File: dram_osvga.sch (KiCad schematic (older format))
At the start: 2 parts

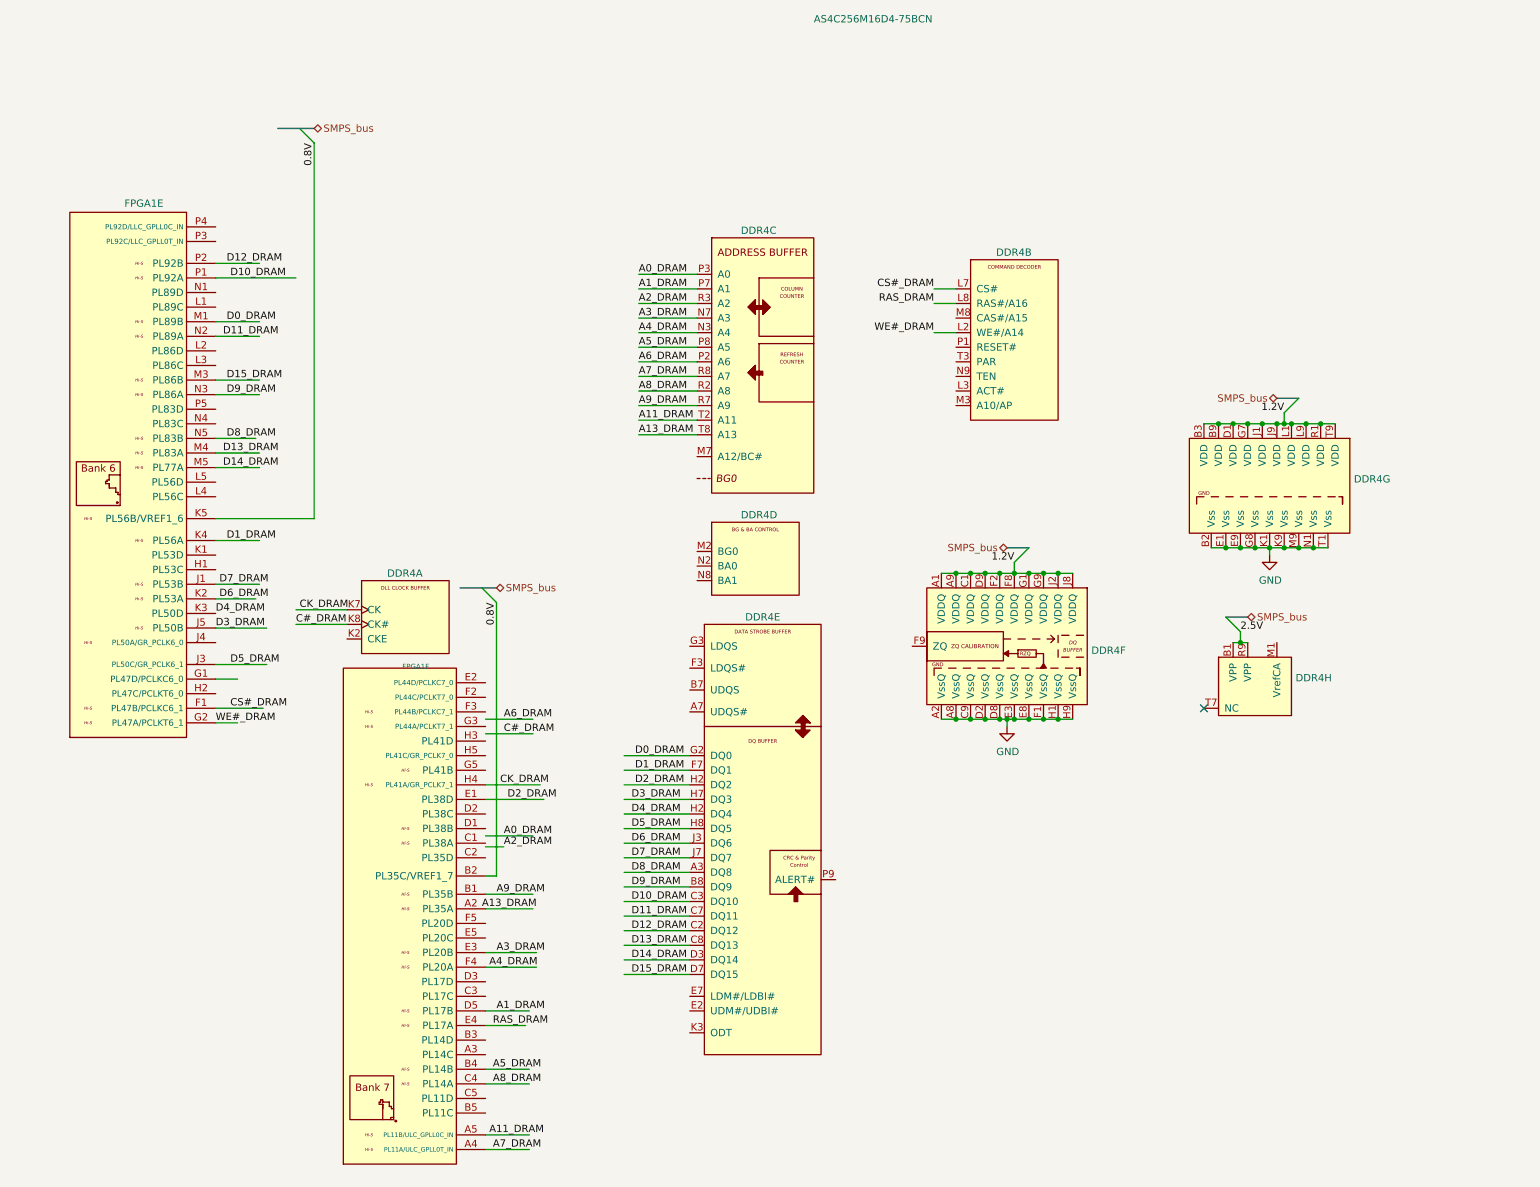
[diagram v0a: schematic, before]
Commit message: Add files via upload
Added Pull-up and pull-down resistors for JTAG and sysConfig connections.
Added pinheaders for FPGA-Configuration. (replacing edge-connector)
Combined the DVI+VGA and USB-C hierarchical sheets into one.
Assigned a dedicated sheet for the DAC.
Added 75 Ohm terminal-resistors to output of DAC.
Placed filtering-capacitors for DAC VAA.
Connected VGA ID-bits and DVI DDC together.
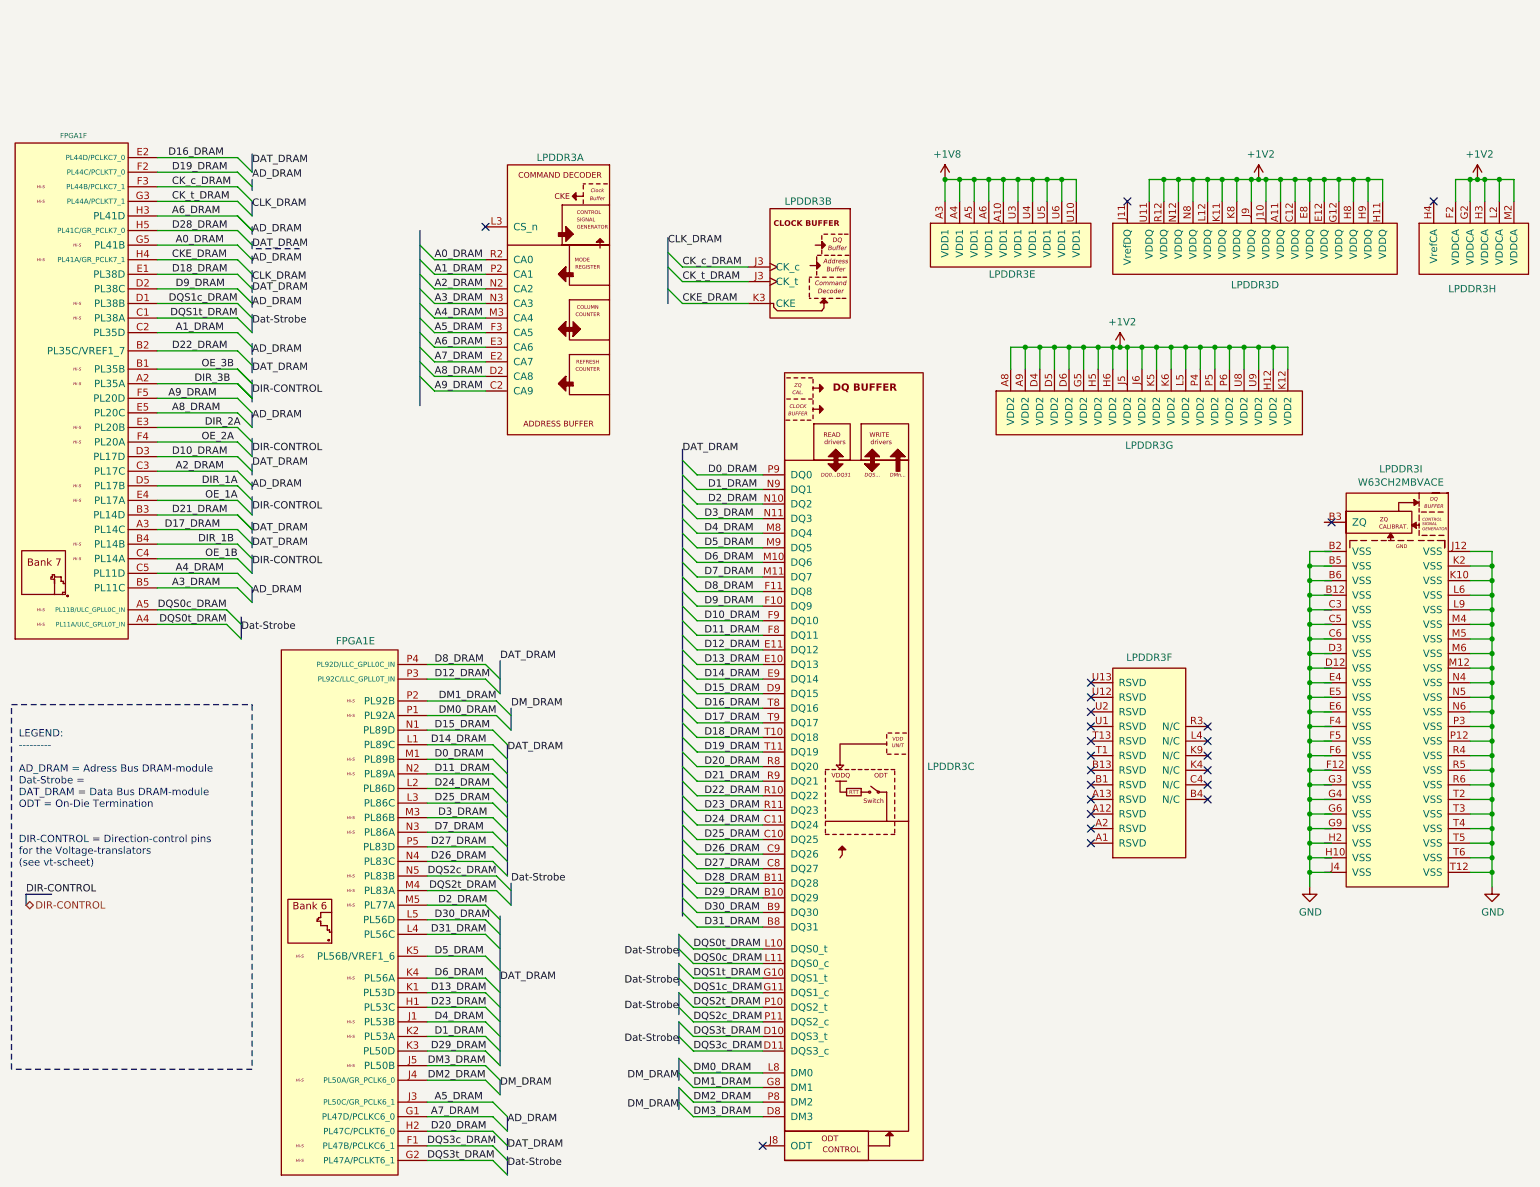
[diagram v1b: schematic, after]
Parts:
- removed DDR4: AS4C256M16D4-75BCN, Package_BGA:FBGA-96-Alliance_, symbol LRJ-parts:AS4C256M16D4-75BCN
- added LPDDR3: W63CH2MBVACE, Package_BGA:Winbond_VFBGA-178_W63CH2MBVACE, symbol LRJ-parts:W63CH2MBVACE
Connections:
- net labels added: +1V2, +1V8, AD_DRAM, CKE_DRAM, CK_c_DRAM, CK_t_DRAM, CLK_DRAM, D16_DRAM, D17_DRAM, D18_DRAM, D19_DRAM, D20_DRAM, D21_DRAM, D22_DRAM, D23_DRAM, D24_DRAM, D25_DRAM, D26_DRAM, D27_DRAM, D28_DRAM, D29_DRAM, D30_DRAM, D31_DRAM, DAT_DRAM, DIR-CONTROL, DIR_1A, DIR_1B, DIR_2A, DIR_3B, DM0_DRAM, DM1_DRAM, DM2_DRAM, DM3_DRAM, DM_DRAM, DQS0c_DRAM, DQS0t_DRAM, DQS1c_DRAM, DQS1t_DRAM, DQS2c_DRAM, DQS2t_DRAM, DQS3c_DRAM, DQS3t_DRAM, Dat-Strobe, OE_1A, OE_1B, OE_2A, OE_3B
- net labels removed: 0.8V, 1.2V, 2.5V, A11_DRAM, A13_DRAM, C#_DRAM, CK_DRAM, CS#_DRAM, RAS_DRAM, SMPS_bus, WE#_DRAM
- wire segments 114 -> 317
- no-connect marks 1 -> 23
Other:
- note added: "LEGEND:\n---------\n\nAD_DRAM = Adress Bus DRAM-module\nDat-Strobe = \nDAT_DRAM = Data Bus DRAM-module\nODT = On-Die Termination\n\n\nDIR-CONTROL = Direction-control pins \nfor the Voltage-translators \n(see vt-scheet)\n\n"
- moved on the sheet: FPGA1E, FPGA1F

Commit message: Add files via upload
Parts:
- added RZQ1: ERJ-8ENF2400V, Resistor_SMD:R_Panasonic_1206_3216Metric_ERJ8EN_HandSolder, symbol LRJ-parts:ERJ-8ENF2400V
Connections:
- net labels added: CON_DRAM, CS_DRAM, ODT_DRAM
- wire segments 317 -> 320
- no-connect marks 23 -> 20
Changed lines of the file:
@@
 $EndComp
 Wire Wire Line
-	9550 3450 9700 3450
-Wire Wire Line
-	9550 3550 9700 3550
-Wire Wire Line
-	9550 3650 9700 3650
-Wire Wire Line
-	9550 3750 9700 3750
-Wire Wire Line
-	9550 3850 9700 3850
-Wire Wire Line
-	9550 3950 9700 3950
-Wire Wire Line
-	9550 4050 9700 4050
-Wire Wire Line
-	9550 4150 9700 4150
-Wire Wire Line
-	9550 4250 9700 4250
-Wire Wire Line
-	9550 4350 9700 4350
-Wire Wire Line
-	9550 4450 9700 4450
-Wire Wire Line
-	9550 4550 9700 4550
-Wire Wire Line
-	9550 4650 9700 4650
-Wire Wire Line
-	9550 4750 9700 4750
-Wire Wire Line
-	9550 4850 9700 4850
-Wire Wire Line
-	9550 4950 9700 4950
-Wire Wire Line
-	9550 5050 9700 5050
-Wire Wire Line
-	9550 5150 9700 5150
-Wire Wire Line
-	9550 5250 9700 5250
-Wire Wire Line
-	9550 5350 9700 5350
-Wire Wire Line
-	9550 5450 9700 5450
-Wire Wire Line
-	9550 5550 9700 5550
-Wire Wire Line
-	9550 5650 9700 5650
+	9500 3450 9650 3450
+Wire Wire Line
+	9500 3550 9650 3550
+Wire Wire Line
+	9500 3650 9650 3650
+Wire Wire Line
+	9500 3750 9650 3750
+Wire Wire Line
+	9500 3850 9650 3850
+Wire Wire Line
+	9500 3950 9650 3950
+Wire Wire Line
+	9500 4050 9650 4050
+Wire Wire Line
+	9500 4150 9650 4150
+Wire Wire Line
+	9500 4250 9650 4250
+Wire Wire Line
+	9500 4350 9650 4350
+Wire Wire Line
+	9500 4450 9650 4450
+Wire Wire Line
+	9500 4550 9650 4550
+Wire Wire Line
+	9500 4650 9650 4650
+Wire Wire Line
+	9500 4750 9650 4750
+Wire Wire Line
+	9500 4850 9650 4850
+Wire Wire Line
+	9500 4950 9650 4950
+Wire Wire Line
+	9500 5050 9650 5050
+Wire Wire Line
+	9500 5150 9650 5150
+Wire Wire Line
+	9500 5250 9650 5250
+Wire Wire Line
+	9500 5350 9650 5350
+Wire Wire Line
+	9500 5450 9650 5450
+Wire Wire Line
+	9500 5550 9650 5550
+Wire Wire Line
+	9500 5650 9650 5650
 Wire Wire Line
 	10650 3450 10800 3450
@@
 L power:GND #PWR0130
 U 1 1 5FC20D0A
-P 9550 5750
-F 0 "#PWR0130" H 9550 5500 50  0001 C CNN
-F 1 "GND" H 9555 5577 50  0000 C CNN
-F 2 "" H 9550 5750 50  0001 C CNN
-F 3 "" H 9550 5750 50  0001 C CNN
-	1    9550 5750
+P 9500 5750
+F 0 "#PWR0130" H 9500 5500 50  0001 C CNN
+F 1 "GND" H 9505 5577 50  0000 C CNN
+F 2 "" H 9500 5750 50  0001 C CNN
+F 3 "" H 9500 5750 50  0001 C CNN
+	1    9500 5750
 	1    0    0    -1
 $EndComp
@@
 $EndComp
 Wire Wire Line
-	9550 3450 9550 3550
-Connection ~ 9550 3550
-Wire Wire Line
-	9550 3550 9550 3650
-Connection ~ 9550 3650
-Wire Wire Line
-	9550 3650 9550 3750
-Connection ~ 9550 3750
-Wire Wire Line
-	9550 3750 9550 3850
-Connection ~ 9550 3850
-Wire Wire Line
-	9550 3850 9550 3950
-Connection ~ 9550 3950
-Wire Wire Line
-	9550 3950 9550 4050
-Connection ~ 9550 4050
-Wire Wire Line
-	9550 4050 9550 4150
-Connection ~ 9550 4150
-Wire Wire Line
-	9550 4150 9550 4250
-Connection ~ 9550 4250
-Wire Wire Line
-	9550 4250 9550 4350
-Connection ~ 9550 4350
-Wire Wire Line
-	9550 4350 9550 4450
-Connection ~ 9550 4450
-Wire Wire Line
-	9550 4450 9550 4550
-Connection ~ 9550 4550
-Wire Wire Line
-	9550 4550 9550 4650
-Connection ~ 9550 4650
-Wire Wire Line
-	9550 4650 9550 4750
-Connection ~ 9550 4750
-Wire Wire Line
-	9550 4750 9550 4850
-Connection ~ 9550 4850
-Wire Wire Line
-	9550 4850 9550 4950
-Connection ~ 9550 4950
-Wire Wire Line
-	9550 4950 9550 5050
-Connection ~ 9550 5050
-Wire Wire Line
-	9550 5050 9550 5150
-Connection ~ 9550 5150
-Wire Wire Line
-	9550 5150 9550 5250
-Connection ~ 9550 5250
-Wire Wire Line
-	9550 5250 9550 5350
-Connection ~ 9550 5350
-Wire Wire Line
-	9550 5350 9550 5450
-Connection ~ 9550 5450
-Wire Wire Line
-	9550 5450 9550 5550
-Connection ~ 9550 5550
-Wire Wire Line
-	9550 5550 9550 5650
-Connection ~ 9550 5650
-Wire Wire Line
-	9550 5650 9550 5750
+	9500 3450 9500 3550
+Connection ~ 9500 3550
+Wire Wire Line
+	9500 3550 9500 3650
+Connection ~ 9500 3650
+Wire Wire Line
+	9500 3650 9500 3750
+Connection ~ 9500 3750
+Wire Wire Line
+	9500 3750 9500 3850
+Connection ~ 9500 3850
+Wire Wire Line
+	9500 3850 9500 3950
+Connection ~ 9500 3950
+Wire Wire Line
+	9500 3950 9500 4050
+Connection ~ 9500 4050
+Wire Wire Line
+	9500 4050 9500 4150
+Connection ~ 9500 4150
+Wire Wire Line
+	9500 4150 9500 4250
+Connection ~ 9500 4250
+Wire Wire Line
+	9500 4250 9500 4350
+Connection ~ 9500 4350
+Wire Wire Line
+	9500 4350 9500 4450
+Connection ~ 9500 4450
+Wire Wire Line
+	9500 4450 9500 4550
+Connection ~ 9500 4550
+Wire Wire Line
+	9500 4550 9500 4650
+Connection ~ 9500 4650
+Wire Wire Line
+	9500 4650 9500 4750
+Connection ~ 9500 4750
+Wire Wire Line
+	9500 4750 9500 4850
+Connection ~ 9500 4850
+Wire Wire Line
+	9500 4850 9500 4950
+Connection ~ 9500 4950
+Wire Wire Line
+	9500 4950 9500 5050
+Connection ~ 9500 5050
+Wire Wire Line
+	9500 5050 9500 5150
+Connection ~ 9500 5150
+Wire Wire Line
+	9500 5150 9500 5250
+Connection ~ 9500 5250
+Wire Wire Line
+	9500 5250 9500 5350
+Connection ~ 9500 5350
+Wire Wire Line
+	9500 5350 9500 5450
+Connection ~ 9500 5450
+Wire Wire Line
+	9500 5450 9500 5550
+Connection ~ 9500 5550
+Wire Wire Line
+	9500 5550 9500 5650
+Connection ~ 9500 5650
+Wire Wire Line
+	9500 5650 9500 5750
 Wire Wire Line
 	10800 3450 10800 3550
@@
 L power:+1V8 #PWR0167
 U 1 1 608605CF
-P 7050 900
-F 0 "#PWR0167" H 7050 750 50  0001 C CNN
-F 1 "+1V8" H 7065 1073 50  0000 C CNN
-F 2 "" H 7050 900 50  0001 C CNN
-F 3 "" H 7050 900 50  0001 C CNN
-	1    7050 900
+P 6975 900
+F 0 "#PWR0167" H 6975 750 50  0001 C CNN
+F 1 "+1V8" H 6990 1073 50  0000 C CNN
+F 2 "" H 6975 900 50  0001 C CNN
+F 3 "" H 6975 900 50  0001 C CNN
+	1    6975 900
 	1    0    0    -1
 $EndComp
@@
 NoConn ~ 8050 5350
 NoConn ~ 8050 5450
-NoConn ~ 3900 1225
-NoConn ~ 5800 7525
-NoConn ~ 9700 3250
 NoConn ~ 10400 1050
 Wire Wire Line
@@
 Text Label 2300 1100 0    50   ~ 0
 CLK_DRAM
-Text Label 2300 900  0    50   ~ 0
-AD_DRAM
 Entry Wire Line
 	2200 850  2300 950
@@
 Wire Wire Line
 	1650 850  2200 850
-Wire Bus Line
-	2300 1050 2300 1150
 Entry Wire Line
 	2200 1250 2300 1350
@@
 Entry Wire Line
 	2200 3200 2300 3300
-Wire Notes Line
-	2325 1375 2625 1375
 Entry Wire Line
 	3950 5075 4050 5175
@@
 Wire Wire Line
 	1650 750  2200 750
-Wire Bus Line
-	2300 725  2300 850
 Text Label 2300 800  0    50   ~ 0
 DAT_DRAM
@@
 	7150 1050 7150 900
 Wire Wire Line
-	7150 900  7250 900
-Connection ~ 7250 900
-Wire Wire Line
 	7250 1050 7250 900
-Wire Wire Line
-	7250 900  7350 900
-Connection ~ 7350 900
 Wire Wire Line
 	7350 1050 7350 900
@@
 Wire Wire Line
 	7650 1050 7650 900
-Connection ~ 7150 900
-Connection ~ 7050 900
 Wire Wire Line
 	7050 900  7150 900
@@
 Text Label 2300 2375 0    50   ~ 0
 DIR-CONTROL
+$Comp
+L LRJ-parts:ERJ-8ENF2400V RZQ1
+U 1 1 5FADDD26
+P 9450 3250
+F 0 "RZQ1" H 9450 3250 39  0000 C CNN
+F 1 "ERJ-8ENF2400V" H 9450 3450 45  0000 C CNN
+F 2 "Resistor_SMD:R_Panasonic_1206_3216Metric_ERJ8EN_HandSolder" H 9450 3400 20  0001 C CNN
+F 3 "https://industrial.panasonic.com/cdbs/www-data/pdf/RDA0000/AOA0000C304.pdf" H 9450 3250 60  0001 C CNN
+F 4 "https://www.mouser.se/datasheet/2/315/AOA0000C304-1149620.pdf" H 11225 3325 50  0001 C CNN "Mouser datasheet"
+F 5 "https://industrial.panasonic.com/ww/products/resistors/chip-resistors/general-purpose-chip-resistors/models/ERJ8ENF2400V" H 12375 3250 50  0001 C CNN "Details"
+F 6 "240Ω" H 9450 3368 43  0000 C CNN "Resistance"
+	1    9450 3250
+	1    0    0    -1
+$EndComp
+$Comp
+L power:GND #PWR0116
+U 1 1 5FAE61DD
+P 9250 3250
+F 0 "#PWR0116" H 9250 3000 50  0001 C CNN
+F 1 "GND" H 9255 3077 50  0000 C CNN
+F 2 "" H 9250 3250 50  0001 C CNN
+F 3 "" H 9250 3250 50  0001 C CNN
+	1    9250 3250
+	1    0    0    -1
+$EndComp
+Wire Wire Line
+	3550 1225 3900 1225
+Entry Wire Line
+	3450 1125 3550 1225
+Wire Wire Line
+	5450 7525 5800 7525
+Entry Wire Line
+	5350 7425 5450 7525
+Wire Bus Line
+	2300 725  2300 850
+Text Label 2300 925  0    50   ~ 0
+DAT_DRAM
+Text Label 3450 2500 0    50   ~ 0
+AD_DRAM
+Text Label 3550 1225 0    50   ~ 0
+CS_DRAM
+Text Label 3450 1075 0    50   ~ 0
+CON_DRAM
+Entry Wire Line
+	5350 7425 5450 7525
+Text Label 5450 7525 0    50   ~ 0
+ODT_DRAM
+Text Label 5350 7675 0    50   ~ 0
+CON_DRAM
+Text HLabel 3450 975  0    50   BiDi ~ 0
+CON_DRAM
+Wire Wire Line
+	6975 900  7050 900
+Connection ~ 7050 900
+Wire Bus Line
+	5350 7375 5350 7675
+Wire Bus Line
+	3450 975  3450 1225
+Wire Bus Line
+	2300 2275 2300 2425
 Wire Bus Line
 	4075 4525 4075 4675
@@
 	4050 7475 4050 7550
 Wire Bus Line
+	4000 5950 4000 6975
+Wire Bus Line
 	4000 4200 4000 4425
 Wire Bus Line
@@
 	2300 1625 2300 1675
 Wire Bus Line
+	4050 4775 4050 5675
+Wire Bus Line
 	2300 1325 2300 1375
 Wire Bus Line
@@
 	2300 1225 2300 1275
 Wire Bus Line
+	2300 1025 2300 1150
+Wire Bus Line
 	2300 900  2300 975
 Wire Bus Line
-	2300 2275 2300 2425
-Wire Bus Line
 	5150 1300 5150 1750
 Wire Bus Line
-	4050 4775 4050 5675
-Wire Bus Line
-	3450 1250 3450 2450
-Wire Bus Line
-	4000 5950 4000 6975
+	3450 1350 3450 2500
 Wire Bus Line
 	5250 2750 5250 5950
+Connection ~ 7150 900
+Wire Wire Line
+	7150 900  7250 900
+Connection ~ 7350 900
+Connection ~ 7250 900
+Wire Wire Line
+	7250 900  7350 900
 $EndSCHEMATC
